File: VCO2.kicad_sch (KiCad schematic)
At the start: 61 parts, among them SW6 SW_SPDT, SW7 SW_SPDT, U6 TL072, U7 TL072, U8 TL072

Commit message: more work...
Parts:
- C? (x4): footprint Capacitor_SMD:C_0805_2012Metric_Pad1.18x1.45mm_HandSolder -> Capacitor_SMD:C_0805_2012Metric
- C? (x7): footprint Capacitor_SMD:C_0805_2012Metric_Pad1.18x1.45mm_HandSolder -> Capacitor_SMD:C_0603_1608Metric
- C?: value 1n -> 1nF; footprint Capacitor_SMD:C_0805_2012Metric_Pad1.18x1.45mm_HandSolder -> Capacitor_SMD:C_0603_1608Metric
- R? (x34): footprint Resistor_SMD:R_0805_2012Metric_Pad1.20x1.40mm_HandSolder -> Resistor_SMD:R_0603_1608Metric
- RV?: footprint Potentiometer_THT:Potentiometer_Alps_RK09K_Single_Vertical -> Potentiometer_SMD:Potentiometer_Bourns_TC33X_Vertical

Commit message: finishing schematic 1.0
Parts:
- SW6, SW7: footprint SynthProjConnectors:ST-0-102-A01-T000-LF -> SynthProjConnectors:MTS-103-A01-T0

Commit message: Doing some layout
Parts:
- removed RV?: 100k, Potentiometer_THT:Potentiometer_Alps_RK09K_Single_Vertical, symbol SynthProj-rescue:R_POT_US-Device
- added RV11: 100k, Potentiometer_SMD:Potentiometer_Bourns_TC33X_Vertical, symbol SynthProj-rescue:R_POT_US-Device
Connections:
- net at D?.1 (K): now also RV11.1
- net at R?.1: now also RV11.2, RV11.3
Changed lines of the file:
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@@
   (junction (at 193.04 114.3) (diameter 0) (color 0 0 0 0)
   )
-  (junction (at 134.62 62.23) (diameter 0) (color 0 0 0 0)
-  )
   (junction (at 177.8 138.43) (diameter 0) (color 0 0 0 0)
   )
@@
   (junction (at 127 95.25) (diameter 0) (color 0 0 0 0)
   )
+  (junction (at 134.62 62.23) (diameter 0) (color 0 0 0 0)
+  )
   (junction (at 76.2 88.9) (diameter 0) (color 0 0 0 0)
   )
@@
     )
   )
-  (symbol (lib_id "SynthProj-rescue:R_POT_US-Device") (at 130.81 62.23 90) (unit 1)
-    (in_bom yes) (on_board yes) (dnp no)
-    (property "Reference" "RV?" (at 129.6416 63.9318 0)
-      (effects (font (size 1.27 1.27)) (justify right))
-    )
-    (property "Value" "100k" (at 131.953 63.9318 0)
-      (effects (font (size 1.27 1.27)) (justify right))
-    )
-    (property "Footprint" "Potentiometer_THT:Potentiometer_Alps_RK09K_Single_Vertical" (at 130.81 62.23 0)
-      (effects (font (size 1.27 1.27)) hide)
-    )
-    (property "Datasheet" "~" (at 130.81 62.23 0)
-      (effects (font (size 1.27 1.27)) hide)
-    )
-    (pin "3")
-    (pin "2")
-    (pin "1")
-    (instances
-      (project "SynthProj"
-        (path "/9021c97e-351f-4ed9-b393-50257df6a463/00000000-0000-0000-0000-0000659d0967"
-          (reference "RV?") (unit 1)
-        )
-        (path "/9021c97e-351f-4ed9-b393-50257df6a463/00000000-0000-0000-0000-0000659a4e2e"
-          (reference "RV?") (unit 1)
-        )
-        (path "/9021c97e-351f-4ed9-b393-50257df6a463/00000000-0000-0000-0000-000065ec1a9f"
-          (reference "RV16") (unit 1)
-        )
-        (path "/9021c97e-351f-4ed9-b393-50257df6a463"
-          (reference "RV?") (unit 1)
-        )
-      )
-    )
-  )
   (symbol (lib_id "Device:R_US") (at 143.51 62.23 90) (unit 1)
     (in_bom yes) (on_board yes) (dnp no)
@@
         )
       )
+    )
+  )
+  (symbol (lib_id "SynthProj-rescue:R_POT_US-Device") (at 130.81 62.23 90) (unit 1)
+    (in_bom yes) (on_board yes) (dnp no)
+    (property "Reference" "RV11" (at 129.6416 63.9318 0)
+      (effects (font (size 1.27 1.27)) (justify right))
+    )
+    (property "Value" "100k" (at 131.953 63.9318 0)
+      (effects (font (size 1.27 1.27)) (justify right))
+    )
+    (property "Footprint" "Potentiometer_SMD:Potentiometer_Bourns_TC33X_Vertical" (at 130.81 62.23 0)
+      (effects (font (size 1.27 1.27)) hide)
+    )
+    (property "Datasheet" "~" (at 130.81 62.23 0)
+      (effects (font (size 1.27 1.27)) hide)
+    )
+    (pin "2")
+    (pin "1")
+    (pin "3")
+    (instances
+      (project "SynthProj"
+        (path "/9021c97e-351f-4ed9-b393-50257df6a463/00000000-0000-0000-0000-0000659d0967"
+          (reference "RV11") (unit 1)
+        )
+        (path "/9021c97e-351f-4ed9-b393-50257df6a463/00000000-0000-0000-0000-0000659a4e2e"
+          (reference "RV?") (unit 1)
+        )
+        (path "/9021c97e-351f-4ed9-b393-50257df6a463"
+          (reference "RV?") (unit 1)
+        )
+        (path "/9021c97e-351f-4ed9-b393-50257df6a463/00000000-0000-0000-0000-000065ec1a9f"
+          (reference "RV16") (unit 1)
+        )
+      )

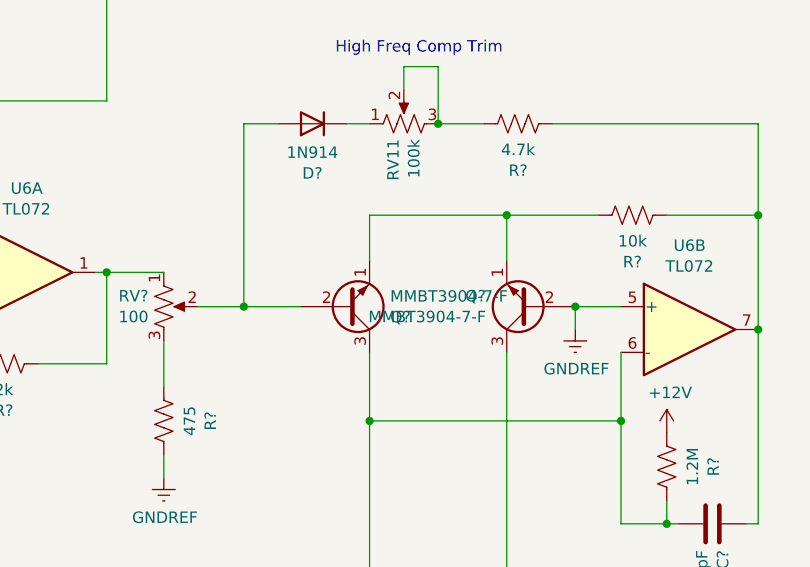
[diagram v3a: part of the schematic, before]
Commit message: doing some routing - split sequencer into another project
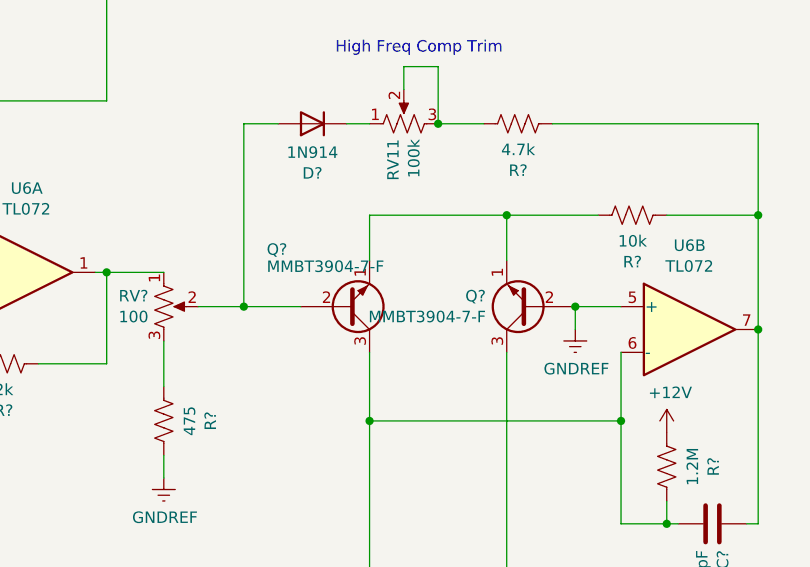
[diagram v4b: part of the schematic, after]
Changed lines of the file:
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@@
   (symbol (lib_id "Transistor_BJT:2N3904") (at 124.46 82.55 0) (mirror x) (unit 1)
     (in_bom yes) (on_board yes) (dnp no)
-    (property "Reference" "Q?" (at 129.286 83.7184 0)
+    (property "Reference" "Q?" (at 115.57 76.2 0)
       (effects (font (size 1.27 1.27)) (justify left))
     )
-    (property "Value" "MMBT3904-7-F" (at 129.286 81.407 0)
+    (property "Value" "MMBT3904-7-F" (at 115.57 78.105 0)
       (effects (font (size 1.27 1.27)) (justify left))
     )

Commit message: lots of routes, added vco3, lfo2.
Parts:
- SW6, SW7: footprint SynthProjConnectors:MTS-103-A01-T0 -> SynthProjConnectors:SMTS-102
